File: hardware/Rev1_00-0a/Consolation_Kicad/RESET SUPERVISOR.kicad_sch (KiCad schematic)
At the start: 27 parts, among them Q10 SSM3K56FS,LF, Q11 SSM3K56FS,LF, U15 SN65DSI84ZXHR, U16 SN74LVC1G125DBVR

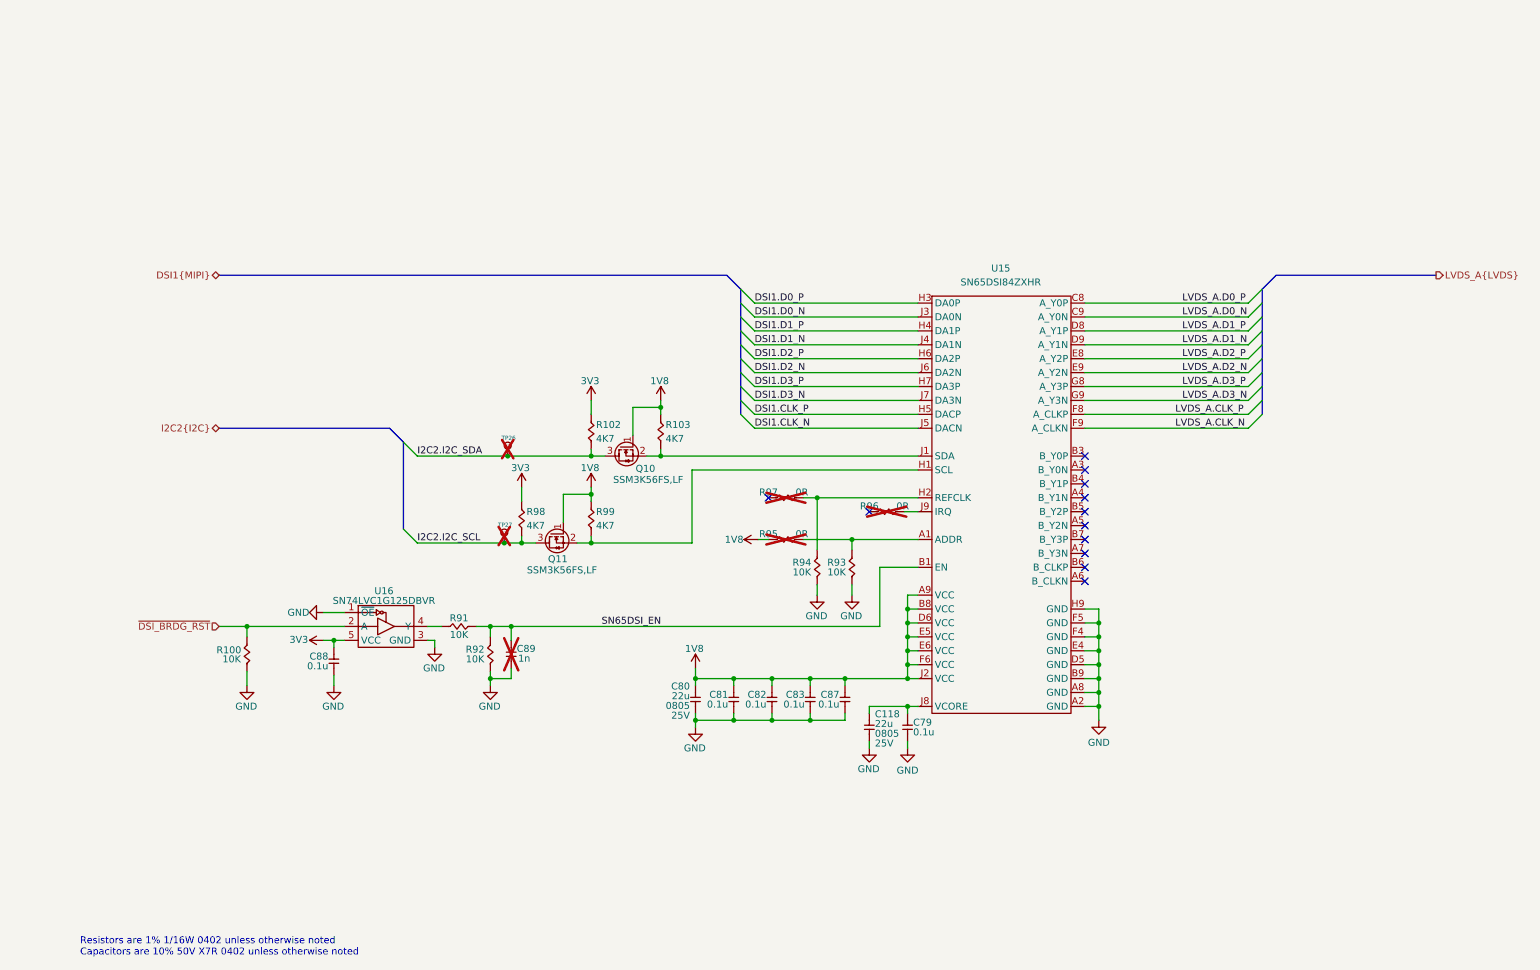
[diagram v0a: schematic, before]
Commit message: Major update to consolation schematics to include - Power supply - RESET SUPERVISOR - Review of GPIO and pinmux
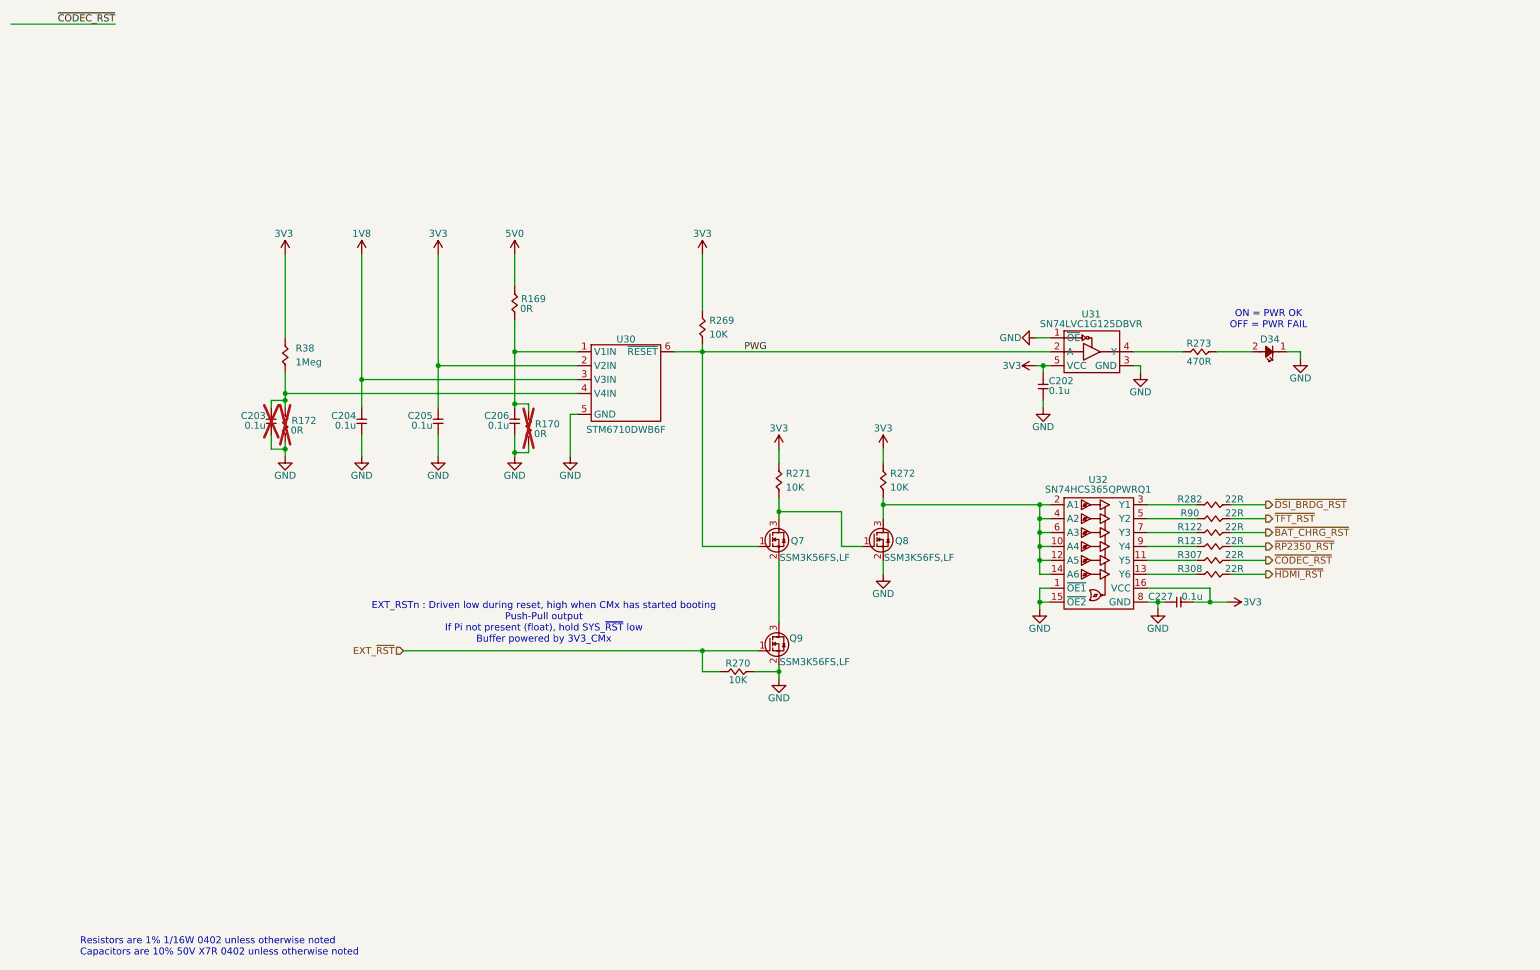
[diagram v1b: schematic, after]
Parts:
- removed C118, C80: 22u, footprint:CAP_NONPOL_0805, symbol KicadCompDb:Capacitors/CAP_CER_SMT_00011
- removed C79, C81, C82, C83, C87, C88: 0.1u, footprint:CAP_NONPOL_0402, symbol KicadCompDb:Capacitors/CAP_CER_SMT_00001
- removed C89: 1n, footprint:CAP_NONPOL_0402, symbol KicadCompDb:Capacitors/CAP_CER_SMT_00005
- removed Q10, Q11: SSM3K56FS,LF, footprint:SC-75, symbol KicadCompDb:Mosfet/MOSFET_00002
- removed R100, R91, R92, R93, R94: 10K, footprint:RES_0402, symbol KicadCompDb:Resistors/RES_SMT_00013
- removed R102, R103, R98, R99: 4K7, footprint:RES_0402, symbol KicadCompDb:Resistors/RES_SMT_00010
- removed R95, R96, R97: 0R, footprint:RES_0402, symbol KicadCompDb:Resistors/RES_SMT_00001
- removed TP26, TP27: 28 mils, footprint:SMT_TP_28_MILS, symbol KicadCompDb:Test Point/TP_00001
- removed U15: SN65DSI84ZXHR, footprint:NFBGA-64, symbol KicadCompDb:Interface/INTRFX_00001
- removed U16: SN74LVC1G125DBVR, footprint:SOT-23-5, symbol KicadCompDb:Logic/LOGIC_00001
- added C202, C203, C204, C205, C206, C227: 0.1u, footprint:CAP_NONPOL_0402, symbol KicadCompDb:Capacitors/CAP_CER_SMT_00001
- added D34: LTST-C190KGKT, footprint:LED_0603, symbol KicadCompDb:Diodes/DIODE_00007
- added Q7, Q8, Q9: SSM3K56FS,LF, footprint:SC-75, symbol KicadCompDb:Mosfet/MOSFET_00002
- added R122, R123, R282, R307, R308, R90: 22R, footprint:RES_0402, symbol KicadCompDb:Resistors/RES_SMT_00015
- added R169, R170, R172: 0R, footprint:RES_0402, symbol KicadCompDb:Resistors/RES_SMT_00001
- added R269, R270, R271, R272: 10K, footprint:RES_0402, symbol KicadCompDb:Resistors/RES_SMT_00013
- added R273: 470R, footprint:RES_0402, symbol KicadCompDb:Resistors/RES_SMT_00019
- added R38: 1Meg, footprint:RES_0402, symbol KicadCompDb:Resistors/RES_SMT_00006
- added U30: STM6710DWB6F, footprint:SOT-23-6, symbol KicadCompDb:Logic/LOGIC_00004
- added U31: SN74LVC1G125DBVR, footprint:SOT-23-5, symbol KicadCompDb:Logic/LOGIC_00001
- added U32: SN74HCS365QPWRQ1, footprint:TSSOP-16-5.8mm, symbol KicadCompDb:Logic/LOGIC_00006
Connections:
- net 1V8: now also C204.2, U30.3 (V3IN)
- net 3V3: now also C202.2, C205.2, C227.1, R269.2, R271.2, R272.2, R38.2, U30.2 (V2IN), U31.5 (VCC), U32.16 (VCC)
- net GND: now also C202.1, C203.1, C204.1, C205.1, C206.1, C227.2, D34.1 (K), Q8.2 (S), Q9.2 (S), R170.1, R172.1, R270.1, U30.5 (GND), U31.1 (~{OE}), U31.3 (GND), U32.1 (~{OE1}), U32.15 (~{OE2}), U32.8 (GND)
- net ~{DSI_BRDG_RST}: now also R282.2
- new net: C203.2, R172.2, R38.1, U30.4 (V4IN)
- new net: R308.1, U32.13 (Y6)
- new net: Q7.3 (D), Q8.1 (G), R271.1
- new net: R90.1, U32.5 (Y2)
- new net: D34.2 (A), R273.2
- new net: C206.2, R169.1, R170.2, U30.1 (V1IN)
- new net: R122.1, U32.7 (Y3)
- new net: R307.1, U32.11 (Y5)
- new net: Q7.2 (S), Q9.3 (D)
- new net: R123.1, U32.9 (Y4)
- new net: Q8.3 (D), R272.1, U32.10 (A4), U32.12 (A5), U32.14 (A6), U32.2 (A1), U32.4 (A2), U32.6 (A3)
- new net: R282.1, U32.3 (Y1)
- new net: R273.1, U31.4 (Y)
- new net 5V0: R169.2
- new net EXT_~{RST}: Q9.1 (G), R270.2
- new net PWG: Q7.1 (G), R269.1, U30.6 (~{RESET}), U31.2 (A)
- new net ~{BAT_CHRG_RST}: R122.2
- new net ~{CODEC_RST}: R307.2
- new net ~{HDMI_RST}: R308.2
- new net ~{RP2350_RST}: R123.2
- new net ~{TFT_RST}: R90.2
- no-connect marks 12 -> 0
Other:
- note added: "EXT_RSTn : Driven low during reset, high when CMx has started booting Push-Pull output If Pi not present (float), hold SYS_~{RST} low Buffer powered by 3V3_CMx"
- note added: "ON = PWR OK OFF = PWR FAIL"

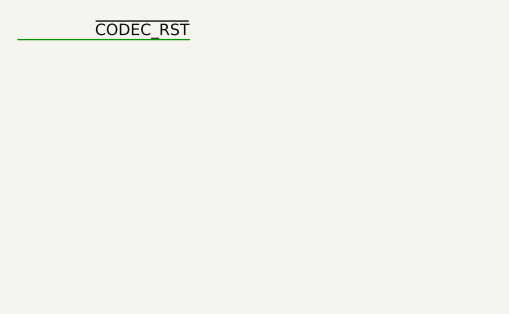
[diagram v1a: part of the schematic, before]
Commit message: Removed unnecessary functions (USB2 mux, CapTouch) Adjusted 220uF alum capacitor for codec (slimmer version)
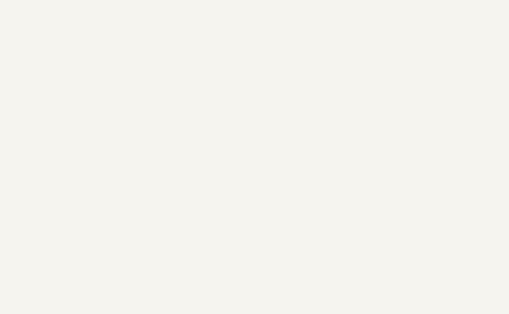
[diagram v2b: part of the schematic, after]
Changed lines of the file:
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@@
-	(wire
-		(pts
-			(xy 19.1262 2.3867) (xy 0.0762 2.3867)
-		)
-		(stroke
-			(width 0)
-			(type default)
-		)
-	)
 	(wire
 		(pts
@@
 			(table_cell "~{PER_RST}"
 				(exclude_from_sim no)
-				(at 137.16 132.08 0)
+				(at 79.375 90.805 0)
 				(size 12.065 2.54)
 				(margins 0.9525 0.9525 0.9525 0.9525)
@@
 			(table_cell "~{EXT_RST}"
 				(exclude_from_sim no)
-				(at 149.225 132.08 0)
+				(at 91.44 90.805 0)
 				(size 11.43 2.54)
 				(margins 0.9525 0.9525 0.9525 0.9525)
@@
 			(table_cell "PWG"
 				(exclude_from_sim no)
-				(at 160.655 132.08 0)
-				(size 11.43 2.54)
-				(margins 0.9525 0.9525 0.9525 0.9525)
-				(span 1 1)
-				(fill
-					(type none)
-				)
-				(effects
-					(font
-						(size 1.27 1.27)
-					)
-					(justify left top)
-				)
-			)
-			(table_cell "0"
-				(exclude_from_sim no)
-				(at 137.16 134.62 0)
+				(at 102.87 90.805 0)
+				(size 11.43 2.54)
+				(margins 0.9525 0.9525 0.9525 0.9525)
+				(span 1 1)
+				(fill
+					(type none)
+				)
+				(effects
+					(font
+						(size 1.27 1.27)
+					)
+					(justify left top)
+				)
+			)
+			(table_cell "0"
+				(exclude_from_sim no)
+				(at 79.375 93.345 0)
 				(size 12.065 2.54)
 				(margins 0.9525 0.9525 0.9525 0.9525)
@@
 			(table_cell "0"
 				(exclude_from_sim no)
-				(at 149.225 134.62 0)
-				(size 11.43 2.54)
-				(margins 0.9525 0.9525 0.9525 0.9525)
-				(span 1 1)
-				(fill
-					(type none)
-				)
-				(effects
-					(font
-						(size 1.27 1.27)
-					)
-					(justify left top)
-				)
-			)
-			(table_cell "0"
-				(exclude_from_sim no)
-				(at 160.655 134.62 0)
-				(size 11.43 2.54)
-				(margins 0.9525 0.9525 0.9525 0.9525)
-				(span 1 1)
-				(fill
-					(type none)
-				)
-				(effects
-					(font
-						(size 1.27 1.27)
-					)
-					(justify left top)
-				)
-			)
-			(table_cell "0"
-				(exclude_from_sim no)
-				(at 137.16 137.16 0)
+				(at 91.44 93.345 0)
+				(size 11.43 2.54)
+				(margins 0.9525 0.9525 0.9525 0.9525)
+				(span 1 1)
+				(fill
+					(type none)
+				)
+				(effects
+					(font
+						(size 1.27 1.27)
+					)
+					(justify left top)
+				)
+			)
+			(table_cell "0"
+				(exclude_from_sim no)
+				(at 102.87 93.345 0)
+				(size 11.43 2.54)
+				(margins 0.9525 0.9525 0.9525 0.9525)
+				(span 1 1)
+				(fill
+					(type none)
+				)
+				(effects
+					(font
+						(size 1.27 1.27)
+					)
+					(justify left top)
+				)
+			)
+			(table_cell "0"
+				(exclude_from_sim no)
+				(at 79.375 95.885 0)
 				(size 12.065 2.54)
 				(margins 0.9525 0.9525 0.9525 0.9525)
@@
 			(table_cell "0"
 				(exclude_from_sim no)
-				(at 149.225 137.16 0)
+				(at 91.44 95.885 0)
 				(size 11.43 2.54)
 				(margins 0.9525 0.9525 0.9525 0.9525)
@@
 			(table_cell "1"
 				(exclude_from_sim no)
-				(at 160.655 137.16 0)
-				(size 11.43 2.54)
-				(margins 0.9525 0.9525 0.9525 0.9525)
-				(span 1 1)
-				(fill
-					(type none)
-				)
-				(effects
-					(font
-						(size 1.27 1.27)
-					)
-					(justify left top)
-				)
-			)
-			(table_cell "0"
-				(exclude_from_sim no)
-				(at 137.16 139.7 0)
+				(at 102.87 95.885 0)
+				(size 11.43 2.54)
+				(margins 0.9525 0.9525 0.9525 0.9525)
+				(span 1 1)
+				(fill
+					(type none)
+				)
+				(effects
+					(font
+						(size 1.27 1.27)
+					)
+					(justify left top)
+				)
+			)
+			(table_cell "0"
+				(exclude_from_sim no)
+				(at 79.375 98.425 0)
 				(size 12.065 2.54)
 				(margins 0.9525 0.9525 0.9525 0.9525)
@@
 			(table_cell "1"
 				(exclude_from_sim no)
-				(at 149.225 139.7 0)
-				(size 11.43 2.54)
-				(margins 0.9525 0.9525 0.9525 0.9525)
-				(span 1 1)
-				(fill
-					(type none)
-				)
-				(effects
-					(font
-						(size 1.27 1.27)
-					)
-					(justify left top)
-				)
-			)
-			(table_cell "0"
-				(exclude_from_sim no)
-				(at 160.655 139.7 0)
+				(at 91.44 98.425 0)
+				(size 11.43 2.54)
+				(margins 0.9525 0.9525 0.9525 0.9525)
+				(span 1 1)
+				(fill
+					(type none)
+				)
+				(effects
+					(font
+						(size 1.27 1.27)
+					)
+					(justify left top)
+				)
+			)
+			(table_cell "0"
+				(exclude_from_sim no)
+				(at 102.87 98.425 0)
 				(size 11.43 2.54)
 				(margins 0.9525 0.9525 0.9525 0.9525)
@@
 			(table_cell "1"
 				(exclude_from_sim no)
-				(at 137.16 142.24 0)
+				(at 79.375 100.965 0)
 				(size 12.065 2.54)
 				(margins 0.9525 0.9525 0.9525 0.9525)
@@
 			(table_cell "1"
 				(exclude_from_sim no)
-				(at 149.225 142.24 0)
+				(at 91.44 100.965 0)
 				(size 11.43 2.54)
 				(margins 0.9525 0.9525 0.9525 0.9525)
@@
 			(table_cell "1"
 				(exclude_from_sim no)
-				(at 160.655 142.24 0)
-				(size 11.43 2.54)
-				(margins 0.9525 0.9525 0.9525 0.9525)
-				(span 1 1)
-				(fill
-					(type none)
-				)
-				(effects
-					(font
-						(size 1.27 1.27)
-					)
-					(justify left top)
-				)
-			)
-		)
-	)
-	(label "~{CODEC_RST}"
-		(at 19.1262 2.3867 180)
-		(effects
-			(font
-				(size 1.27 1.27)
-			)
-			(justify right bottom)
-		)
-	)
+				(at 102.87 100.965 0)
+				(size 11.43 2.54)
+				(margins 0.9525 0.9525 0.9525 0.9525)
+				(span 1 1)
+				(fill
+					(type none)
+				)
+				(effects
+					(font
+						(size 1.27 1.27)
+					)
+					(justify left top)
+				)
+			)
+		)
+	)
